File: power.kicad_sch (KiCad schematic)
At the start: 9 parts, among them J20 Screw_Terminal_01x02, U6 AMS1117-3.3

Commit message: ongoing add MCU and radio.
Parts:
- C15, C16, C5, C6, C7, C8: MountType (none) -> SMT
- D3: symbol Diode:BAT54C -> ProjectLib:BAT54C; MountType (none) -> SMT; Notes (none) -> or equivqalent
- J20: MountType (none) -> PTH
- U6: symbol Regulator_Linear:AMS1117-3.3 -> ProjectLib:AMS1117-3.3; Manufacturer (none) -> Advanced Monolithic; MfgPart (none) -> AMS1117-3.3; MountType (none) -> SMT; Notes (none) -> or equivalent
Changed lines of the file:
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@@
-	)
-	(junction
-		(at 104.14 64.77)
-		(diameter 0)
-		(color 0 0 0 0)
 	)
 	(junction
@@
 	)
 	(junction
-		(at 129.54 118.11)
-		(diameter 0)
-		(color 0 0 0 0)
-	)
-	(junction
 		(at 102.87 95.25)
 		(diameter 0)
@@
 	)
 	(junction
+		(at 104.14 74.93)
+		(diameter 0)
+		(color 0 0 0 0)
+	)
+	(junction
 		(at 95.25 87.63)
 		(diameter 0)
@@
 	)
 	(junction
+		(at 121.92 118.11)
+		(diameter 0)
+		(color 0 0 0 0)
+	)
+	(junction
 		(at 156.21 95.25)
 		(diameter 0)
@@
 	(wire
 		(pts
-			(xy 121.92 118.11) (xy 129.54 118.11)
-		)
-		(stroke
-			(width 0)
-			(type default)
-		)
-	)
-	(wire
-		(pts
 			(xy 146.05 87.63) (xy 137.16 87.63)
 		)
@@
 	(wire
 		(pts
-			(xy 96.52 64.77) (xy 104.14 64.77)
-		)
-		(stroke
-			(width 0)
-			(type default)
-		)
-	)
-	(wire
-		(pts
-			(xy 104.14 64.77) (xy 104.14 74.93)
+			(xy 104.14 71.12) (xy 104.14 74.93)
 		)
 		(stroke
@@
 	(wire
 		(pts
-			(xy 104.14 62.23) (xy 104.14 64.77)
-		)
-		(stroke
-			(width 0)
-			(type default)
-		)
-	)
-	(wire
-		(pts
 			(xy 151.13 73.66) (xy 130.81 73.66)
 		)
@@
 	(wire
 		(pts
-			(xy 129.54 118.11) (xy 137.16 118.11)
+			(xy 121.92 118.11) (xy 137.16 118.11)
 		)
 		(stroke
@@
 	(wire
 		(pts
-			(xy 129.54 115.57) (xy 129.54 118.11)
-		)
-		(stroke
-			(width 0)
-			(type default)
-		)
-	)
-	(wire
-		(pts
 			(xy 137.16 87.63) (xy 111.76 87.63)
 		)
@@
 		(pts
 			(xy 85.09 87.63) (xy 95.25 87.63)
+		)
+		(stroke
+			(width 0)
+			(type default)
+		)
+	)
+	(wire
+		(pts
+			(xy 121.92 118.11) (xy 121.92 121.92)
 		)
 		(stroke
@@
 			)
 		)
-		(property "Description" ""
+		(property "Description" "Power symbol creates a global label with name \"+3V3\""
 			(at 121.92 116.84 0)
 			(effects
@@
 	(symbol
 		(lib_id "power:PWR_FLAG")
-		(at 129.54 115.57 0)
+		(at 121.92 121.92 0)
+		(mirror x)
 		(unit 1)
 		(exclude_from_sim no)
@@
 		(on_board yes)
 		(dnp no)
-		(fields_autoplaced yes)
 		(property "Reference" "#FLG02"
-			(at 129.54 113.665 0)
+			(at 121.92 123.825 0)
 			(effects
 				(font
@@
 		)
 		(property "Value" "PWR_FLAG"
-			(at 129.54 110.49 0)
+			(at 121.92 127 0)
 			(effects
 				(font
@@
 		)
 		(property "Footprint" ""
-			(at 129.54 115.57 0)
+			(at 121.92 121.92 0)
 			(effects
 				(font
@@
 		)
 		(property "Datasheet" "~"
-			(at 129.54 115.57 0)
-			(effects
-				(font
-					(size 1.27 1.27)
-				)
-				(hide yes)
-			)
-		)
-		(property "Description" ""
-			(at 129.54 115.57 0)
+			(at 121.92 121.92 0)
+			(effects
+				(font
+					(size 1.27 1.27)
+				)
+				(hide yes)
+			)
+		)
+		(property "Description" "Special symbol for telling ERC where power comes from"
+			(at 121.92 121.92 0)
 			(effects
 				(font
@@
 	)
 	(symbol
-		(lib_id "Regulator_Linear:AMS1117-3.3")
+		(lib_id "ProjectLib:AMS1117-3.3")
 		(at 153.67 86.36 180)
 		(unit 1)
@@
 			)
 		)
+		(property "Manufacturer" "Advanced Monolithic"
+			(at 153.67 86.36 0)
+			(effects
+				(font
+					(size 1.27 1.27)
+				)
+				(hide yes)
+			)
+		)
+		(property "MfgPart" "AMS1117-3.3 "
+			(at 153.67 86.36 0)
+			(effects
+				(font
+					(size 1.27 1.27)
+				)
+				(hide yes)
+			)
+		)
+		(property "MountType" "SMT"
+			(at 153.67 86.36 0)
+			(effects
+				(font
+					(size 1.27 1.27)
+				)
+				(hide yes)
+			)
+		)
+		(property "Notes" "or equivalent"
+			(at 153.67 86.36 0)
+			(effects
+				(font
+					(size 1.27 1.27)
+				)
+				(hide yes)
+			)
+		)
 		(pin "3"
 		)
@@
 	(symbol
 		(lib_id "power:GND")
-		(at 96.52 64.77 0)
+		(at 104.14 74.93 0)
 		(unit 1)
 		(exclude_from_sim no)
@@
 		(fields_autoplaced yes)
 		(property "Reference" "#PWR041"
-			(at 96.52 71.12 0)
+			(at 104.14 81.28 0)
 			(effects
 				(font
@@
 		)
 		(property "Value" "GND"
-			(at 96.52 69.85 0)
+			(at 104.14 80.01 0)
 			(effects
 				(font
@@
 		)
 		(property "Footprint" ""
-			(at 96.52 64.77 0)
+			(at 104.14 74.93 0)
 			(effects
 				(font
@@
 		)
 		(property "Datasheet" ""
-			(at 96.52 64.77 0)
-			(effects
-				(font
-					(size 1.27 1.27)
-				)
-				(hide yes)
-			)
-		)
-		(property "Description" ""
-			(at 96.52 64.77 0)
+			(at 104.14 74.93 0)
+			(effects
+				(font
+					(size 1.27 1.27)
+				)
+				(hide yes)
+			)
+		)
+		(property "Description" "Power symbol creates a global label with name \"GND\" , ground"
+			(at 104.14 74.93 0)
 			(effects
 				(font
@@
 	(symbol
 		(lib_id "power:PWR_FLAG")
-		(at 104.14 62.23 0)
+		(at 104.14 71.12 0)
 		(unit 1)
 		(exclude_from_sim no)
@@
 		(dnp no)
 		(property "Reference" "#FLG01"
-			(at 104.14 60.325 0)
+			(at 104.14 69.215 0)
 			(effects
 				(font
@@
 		)
 		(property "Value" "PWR_FLAG"
-			(at 104.14 57.15 0)
+			(at 104.14 66.04 0)
 			(effects
 				(font
@@
 		)
 		(property "Footprint" ""
-			(at 104.14 62.23 0)
+			(at 104.14 71.12 0)
 			(effects
 				(font
@@
 		)
 		(property "Datasheet" "~"
-			(at 104.14 62.23 0)
-			(effects
-				(font
-					(size 1.27 1.27)
-				)
-				(hide yes)
-			)
-		)
-		(property "Description" ""
-			(at 104.14 62.23 0)
+			(at 104.14 71.12 0)
+			(effects
+				(font
+					(size 1.27 1.27)
+				)
+				(hide yes)
+			)
+		)
+		(property "Description" "Special symbol for telling ERC where power comes from"
+			(at 104.14 71.12 0)
 			(effects
 				(font
@@
 			)
 		)
+		(property "MountType" "SMT"
+			(at 111.76 91.44 0)
+			(effects
+				(font
+					(size 1.27 1.27)
+				)
+				(hide yes)
+			)
+		)
 		(pin "1"
 		)
@@
 			)
 		)
+		(property "MountType" "SMT"
+			(at 102.87 91.44 0)
+			(effects
+				(font
+					(size 1.27 1.27)
+				)
+				(hide yes)
+			)
+		)
 		(pin "1"
 		)
@@
 			)
 		)
+		(property "MountType" "PTH"
+			(at 153.67 68.58 0)
+			(effects
+				(font
+					(size 1.27 1.27)
+				)
+				(hide yes)
+			)
+		)
 		(pin "1"
 		)
@@
 	)
 	(symbol
-		(lib_name "GND_1")
 		(lib_id "power:GND")
 		(at 156.21 102.87 0)
@@
 			)
 		)
-		(property "Description" ""
+		(property "Description" "Power symbol creates a global label with name \"GND\" , ground"
 			(at 115.57 95.25 0)
 			(effects
@@
 			)
 		)
+		(property "MountType" "SMT"
+			(at 85.09 91.44 0)
+			(effects
+				(font
+					(size 1.27 1.27)
+				)
+				(hide yes)
+			)
+		)
 		(pin "1"
 		)
@@
 	)
 	(symbol
-		(lib_id "Diode:BAT54C")
+		(lib_id "ProjectLib:BAT54C")
 		(at 144.78 118.11 0)
 		(mirror x)
@@
 		)
 		(property "Description" "dual schottky barrier diode, common cathode"
+			(at 144.78 118.11 0)
+			(effects
+				(font
+					(size 1.27 1.27)
+				)
+				(hide yes)
+			)
+		)
+		(property "MountType" "SMT"
+			(at 144.78 118.11 0)
+			(effects
+				(font
+					(size 1.27 1.27)
+				)
+				(hide yes)
+			)
+		)
+		(property "Notes" "or equivqalent"
 			(at 144.78 118.11 0)
 			(effects
@@
 		)
 		(property "Description" "Unpolarized capacitor"
+			(at 156.21 99.06 0)
+			(effects
+				(font
+					(size 1.27 1.27)
+				)
+				(hide yes)
+			)
+		)
+		(property "MountType" "SMT"
 			(at 156.21 99.06 0)
 			(effects
@@
 			)
 		)
+		(property "MountType" "SMT"
+			(at 119.38 71.12 0)
+			(effects
+				(font
+					(size 1.27 1.27)
+				)
+				(hide yes)
+			)
+		)
 		(pin "2"
 		)
@@
 			(at 95.25 91.44 0)
 			(effects
+				(font
+					(size 1.27 1.27)
+				)
+				(hide yes)
+			)
+		)
+		(property "MountType" "SMT"
+			(at 95.25 91.44 0)
+			(effects

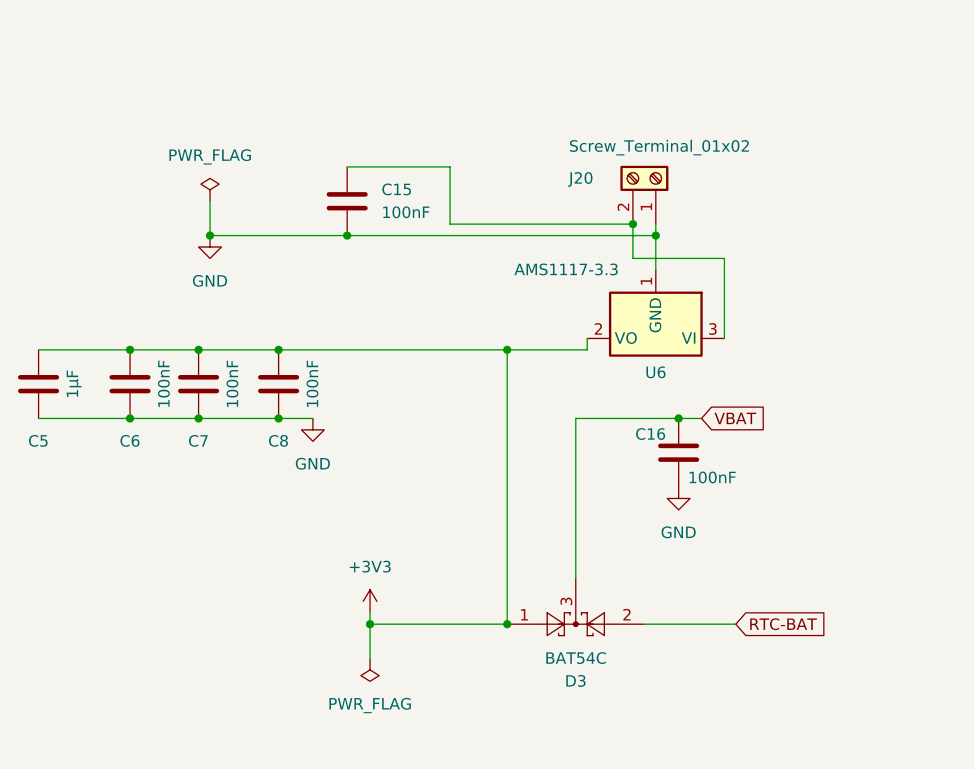
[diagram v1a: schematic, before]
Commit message: ERC passing, Crytals not specified. Considering reverse polarity safeguard.
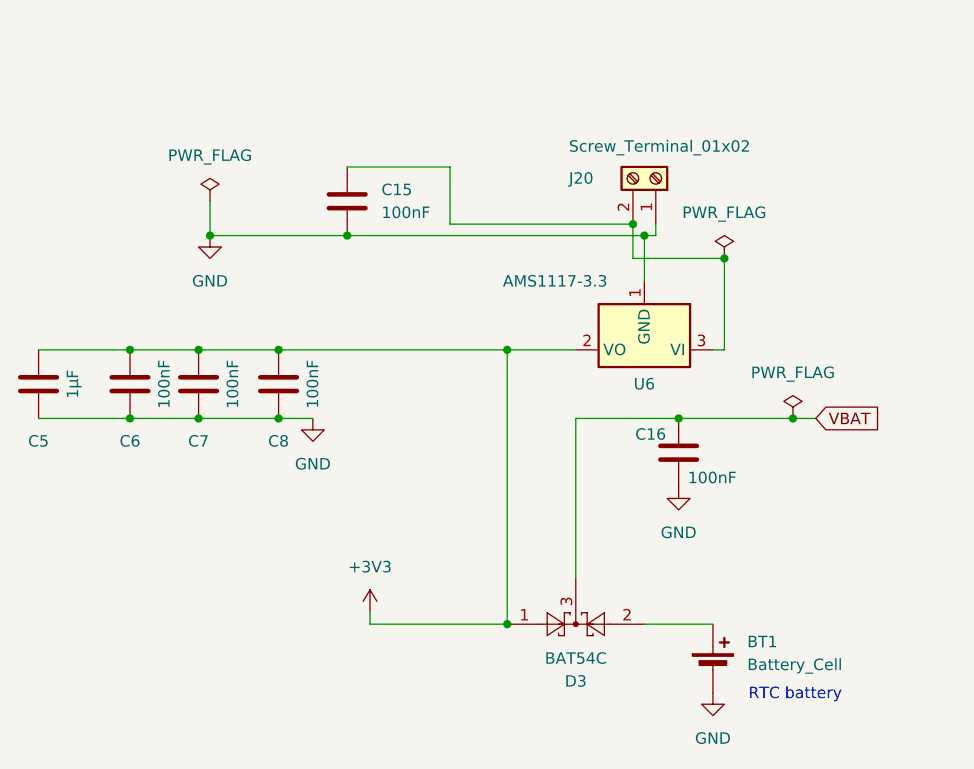
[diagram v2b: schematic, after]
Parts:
- added BT1: Battery_Cell, symbol Device:Battery_Cell
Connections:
- net GND: now also BT1.2 (-)
- net RTC-BAT: no longer names the net of D3.2
- net RTC-BAT: now also BT1.1 (+)
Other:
- note added: "RTC battery"
- moved on the sheet: U6

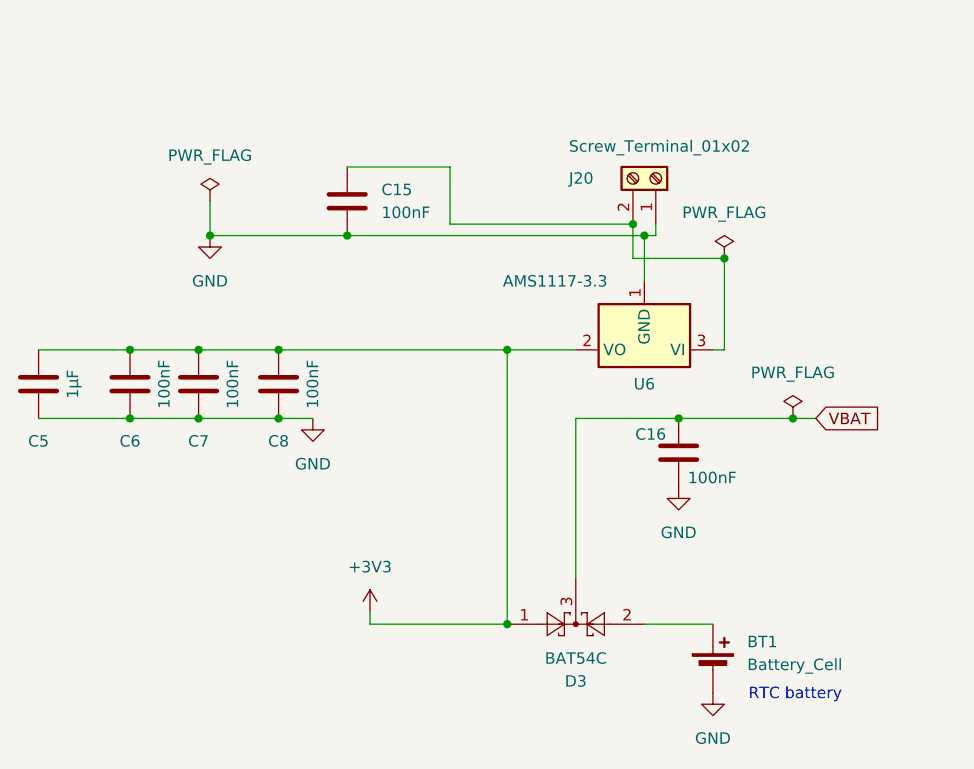
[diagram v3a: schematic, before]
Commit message: layout with F411 roughly good but needs work.
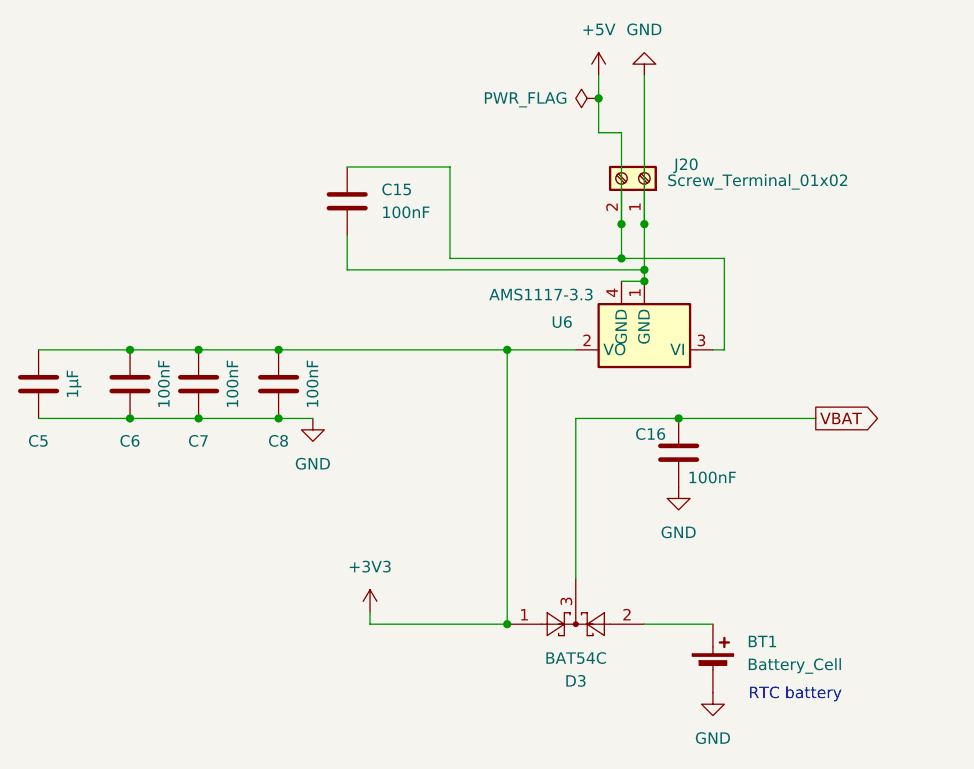
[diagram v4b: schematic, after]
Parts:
- removed BT1: Battery_Cell, symbol Device:Battery_Cell
- added BT1: Battery_Cell, ProjectLib:Battery_Panasonic_CR1025-VSK_Vertical_CircularHoles, symbol ProjectLib:Battery_Cell
- C15, C16, C5, C6, C7, C8: footprint ProjectLib:C_0805_2012Metric -> ProjectLib:C_0603_1608Metric
- D3: footprint Package_TO_SOT_SMD:SOT-23 -> ProjectLib:SOT-23; Manufacturer (none) -> Diodes Inc.; MfgPart (none) -> BAT54C
- U6: footprint Package_TO_SOT_SMD:SOT-223-3_TabPin2 -> ProjectLib:SOT-223
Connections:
- net GND: now also U6.4 (GND), BT1.2 (-)
- net +5V: now reaches C15.1, J20.2 (Pin_2), U6.3 (VI)
- net at D3.2: now also BT1.1 (+)
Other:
- moved on the sheet: J20

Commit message: battery needs work.
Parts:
- BT1: footprint ProjectLib:Battery_Panasonic_CR1025-VSK_Vertical_CircularHoles -> ProjectLib:BatteryHolder_LINX_BAT-HLD-012-SMT
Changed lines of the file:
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@@
 			)
 		)
-		(property "Footprint" "ProjectLib:Battery_Panasonic_CR1025-VSK_Vertical_CircularHoles"
+		(property "Footprint" "ProjectLib:BatteryHolder_LINX_BAT-HLD-012-SMT"
 			(at 160.02 121.666 90)
 			(effects

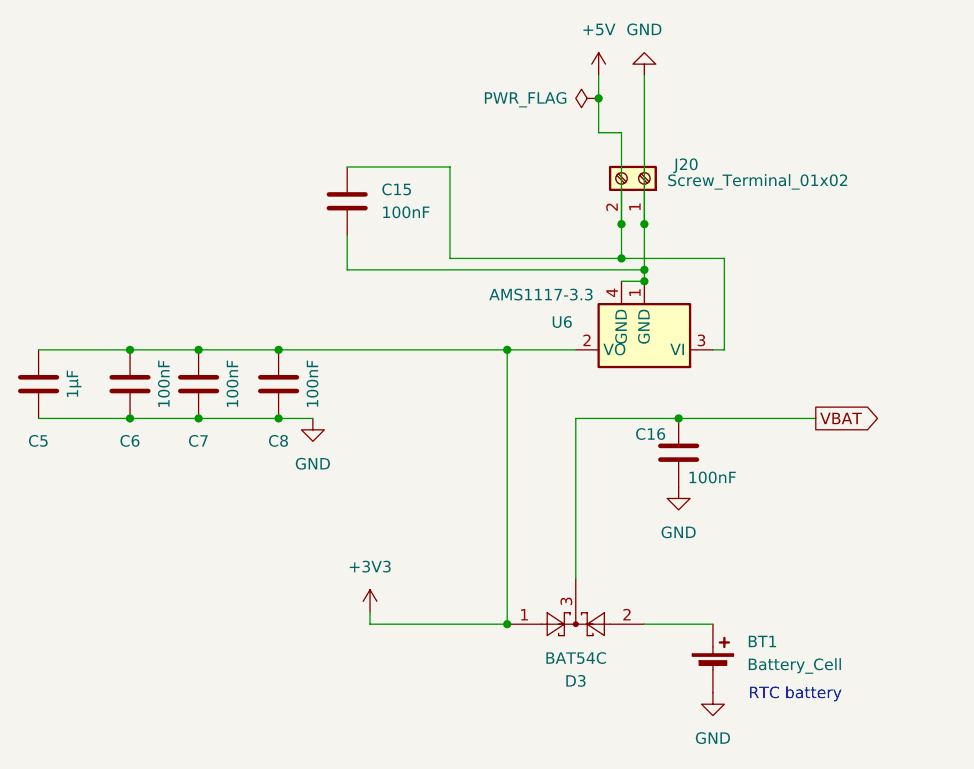
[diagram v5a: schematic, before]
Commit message: near complete, DRC good, ERC has a spurious error about ground on Y1.
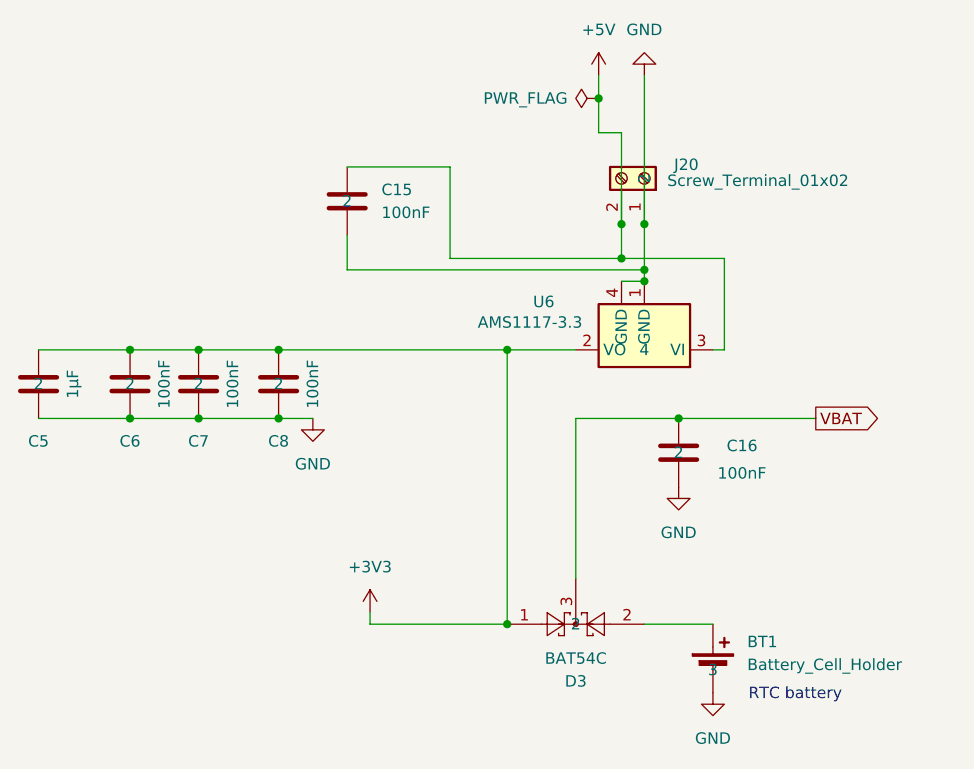
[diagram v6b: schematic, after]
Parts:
- BT1: value Battery_Cell -> Battery_Cell_Holder; Manufacturer (none) -> TE Connectivity Linx; MfgPart (none) -> BAT-HLD-012-SMT; MountType (none) -> SMT; Notes (none) -> or equivalent; pads (none) -> 3
- C15, C16, C5, C6, C7, C8, D3: pads (none) -> 2
- J20: Manufacturer (none) -> Cixi Kefa Elec; MfgPart (none) -> KF128-2.54-2P; Notes (none) -> or equivalent; pads (none) -> 2
- U6: pads (none) -> 4
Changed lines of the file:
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@@
 		(dnp no)
 		(property "Reference" "U6"
-			(at 143.256 84.582 0)
+			(at 141.224 82.296 0)
 			(effects
 				(font
@@
 		)
 		(property "Value" "AMS1117-3.3"
-			(at 140.97 81.534 0)
+			(at 139.7 84.582 0)
 			(effects
 				(font
@@
 				)
 				(hide yes)
+			)
+		)
+		(property "pads" "4"
+			(at 152.4 87.63 0)
+			(effects
+				(font
+					(size 1.27 1.27)
+				)
 			)
 		)
@@
 			)
 		)
+		(property "pads" "2"
+			(at 111.76 91.44 0)
+			(effects
+				(font
+					(size 1.27 1.27)
+				)
+			)
+		)
 		(pin "1"
 		)
@@
 			)
 		)
+		(property "pads" "2"
+			(at 102.87 91.44 0)
+			(effects
+				(font
+					(size 1.27 1.27)
+				)
+			)
+		)
 		(pin "1"
 		)
@@
 		(on_board yes)
 		(dnp no)
-		(fields_autoplaced yes)
 		(property "Reference" "BT1"
 			(at 163.83 120.0784 0)
@@
 			)
 		)
-		(property "Value" "Battery_Cell"
+		(property "Value" "Battery_Cell_Holder"
 			(at 163.83 122.6184 0)
 			(effects
@@
 			)
 		)
-		(property "Datasheet" "~"
+		(property "Datasheet" "~https://www.te.com/commerce/DocumentDelivery/DDEController?Action=srchrtrv&DocNm=BAT-HLD-012-SMT&DocType=Data+Sheet&DocLang=English&DocFormat=pdf&PartCntxt=BAT-HLD-012-SMT"
 			(at 160.02 121.666 90)
 			(effects
@@
 			)
 		)
-		(property "Description" "Single-cell battery"
+		(property "Description" "battery retainer coin 12mm smd"
 			(at 160.02 123.19 0)
 			(effects
@@
 				)
 				(hide yes)
+			)
+		)
+		(property "Manufacturer" "TE Connectivity Linx"
+			(at 172.72 129.286 0)
+			(effects
+				(font
+					(size 1.27 1.27)
+				)
+				(hide yes)
+			)
+		)
+		(property "MfgPart" "BAT-HLD-012-SMT"
+			(at 171.45 117.602 0)
+			(effects
+				(font
+					(size 1.27 1.27)
+				)
+				(hide yes)
+			)
+		)
+		(property "MountType" "SMT"
+			(at 160.02 123.19 0)
+			(effects
+				(font
+					(size 1.27 1.27)
+				)
+				(hide yes)
+			)
+		)
+		(property "Notes" "or equivalent"
+			(at 172.72 131.572 0)
+			(effects
+				(font
+					(size 1.27 1.27)
+				)
+				(hide yes)
+			)
+		)
+		(property "pads" "3"
+			(at 160.02 123.19 0)
+			(effects
+				(font
+					(size 1.27 1.27)
+				)
 			)
 		)
@@
 			)
 		)
+		(property "Manufacturer" "Cixi Kefa Elec"
+			(at 165.1 70.866 90)
+			(effects
+				(font
+					(size 1.27 1.27)
+				)
+				(hide yes)
+			)
+		)
+		(property "MfgPart" "KF128-2.54-2P"
+			(at 165.1 72.898 90)
+			(effects
+				(font
+					(size 1.27 1.27)
+				)
+				(hide yes)
+			)
+		)
+		(property "Notes" "or equivalent"
+			(at 165.608 74.93 90)
+			(effects
+				(font
+					(size 1.27 1.27)
+				)
+				(hide yes)
+			)
+		)
+		(property "pads" "2"
+			(at 152.4 68.58 0)
+			(effects
+				(font
+					(size 1.27 1.27)
+				)
+			)
+		)
 		(pin "1"
 		)
@@
 			)
 		)
+		(property "pads" "2"
+			(at 85.09 91.44 0)
+			(effects
+				(font
+					(size 1.27 1.27)
+				)
+			)
+		)
 		(pin "1"
 		)
@@
 			)
 		)
+		(property "pads" "2"
+			(at 144.78 118.11 0)
+			(effects
+				(font
+					(size 1.27 1.27)
+				)
+			)
+		)
 		(pin "2"
 		)
@@
 		(dnp no)
 		(property "Reference" "C16"
-			(at 151.384 97.028 0)
+			(at 161.544 98.298 0)
 			(effects
 				(font
@@
 		)
 		(property "Value" "100nF"
-			(at 157.226 101.854 0)
+			(at 160.528 101.346 0)
 			(effects
 				(font
@@
 				)
 				(hide yes)
+			)
+		)
+		(property "pads" "2"
+			(at 156.21 99.06 0)
+			(effects
+				(font
+					(size 1.27 1.27)
+				)
 			)
 		)
@@
 			)
 		)
+		(property "pads" "2"
+			(at 119.38 71.12 0)
+			(effects
+				(font
+					(size 1.27 1.27)
+				)
+			)
+		)
 		(pin "2"
 		)
@@
 			)
 		)
+		(property "pads" "2"
+			(at 95.25 91.44 0)
+			(effects
+				(font
+					(size 1.27 1.27)
+				)
+			)
+		)
